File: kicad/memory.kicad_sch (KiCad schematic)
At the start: 12 parts, among them U10 W65C22S, U11 74AC138, U6 Address_Decoder, U7 AS6C4008, U8 AS6C4008, U9 AT28C256

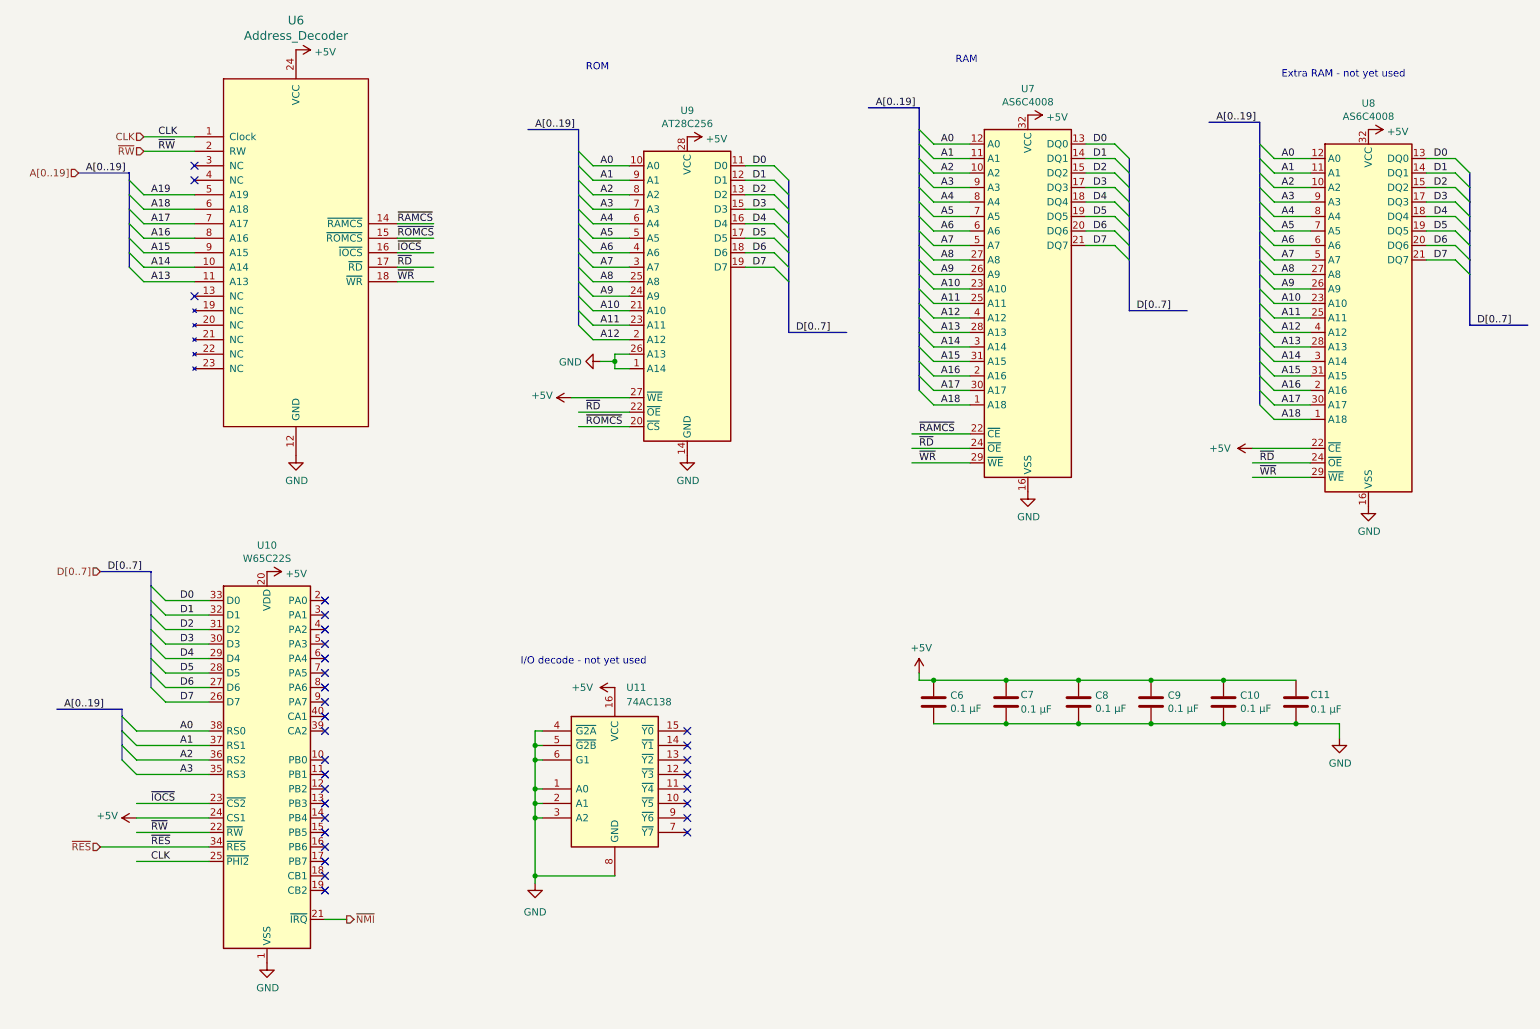
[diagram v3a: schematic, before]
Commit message: update address decoding, extend README
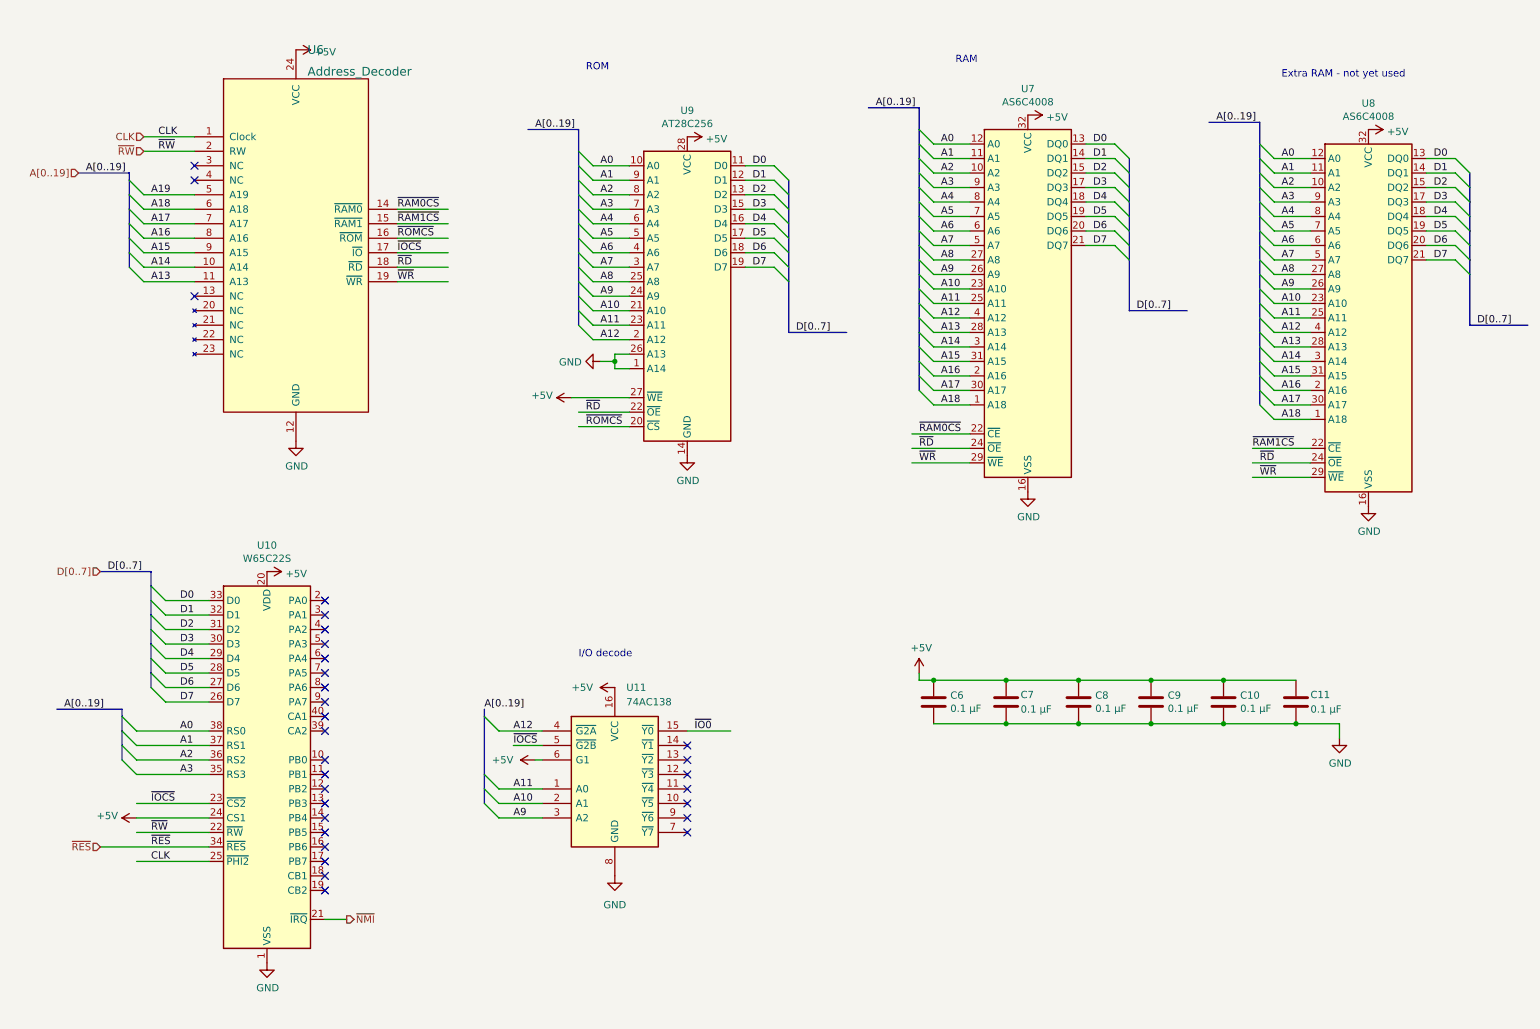
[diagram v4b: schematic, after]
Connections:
- net +5V: now also U11.6 (G1); no longer U8.22 (~{CE})
- net A10: now also U11.2 (A1)
- net A11: now also U11.1 (A0)
- net A12: now also U11.4 (~{G2A})
- net A9: now also U11.3 (A2)
- net GND: no longer U11.1 (A0), U11.2 (A1), U11.3 (A2), U11.4 (~{G2A}), U11.5 (~{G2B}), U11.6 (G1)
- net ~{IOCS}: now also U11.5 (~{G2B}), U6.17 (~{IO}); no longer U6.16 (~{IOCS})
- net ~{RD}: now also U6.18 (~{RD}); no longer U6.17 (~{RD})
- net ~{ROMCS}: now also U6.16 (~{ROM}); no longer U6.15 (~{ROMCS})
- net ~{WR}: now also U6.19 (~{WR}); no longer U6.18 (~{WR})
- net ~{IO0}: now reaches U11.15 (~{Y0})
- net ~{RAMCS} renamed ~{RAM0CS}
- new net ~{RAM1CS}: U6.15 (~{RAM1}), U8.22 (~{CE})
- no-connect marks 31 -> 30
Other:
- note added: "I/O decode"
- note removed: "I/O decode - not yet used"

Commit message: separate I/O schematic page, add SC16C752 for future use
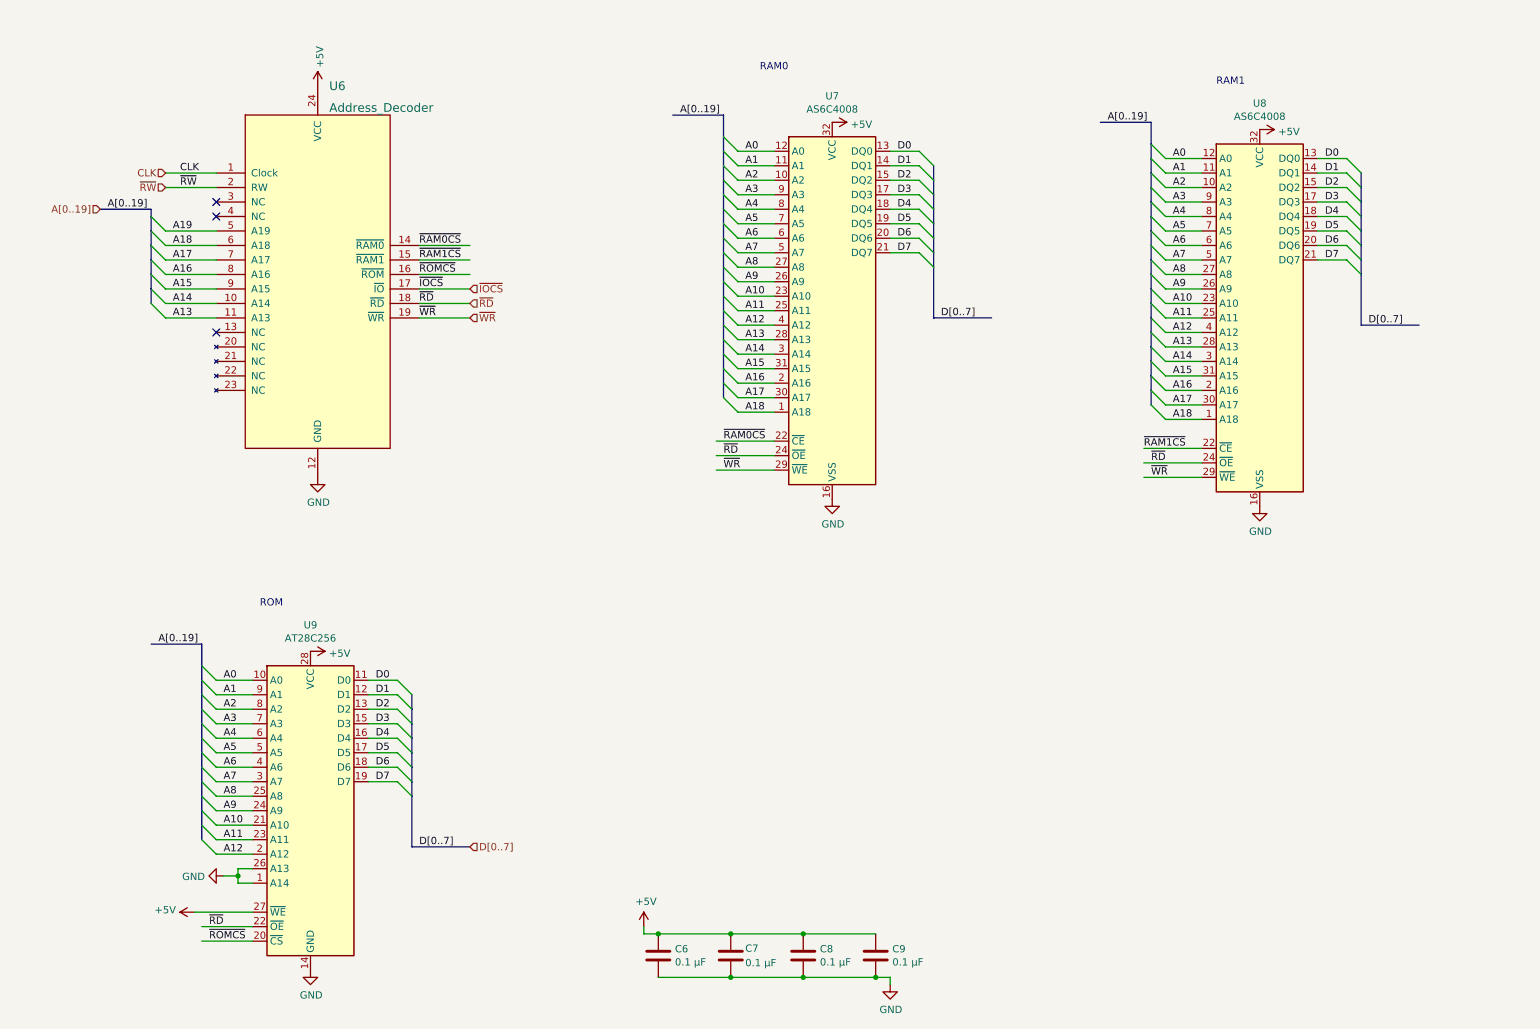
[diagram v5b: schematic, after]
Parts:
- removed C10, C11: 0.1 µF, symbol Device:C
- removed U10: W65C22S, Package_DIP:DIP-40_W15.24mm, symbol project:W65C22S
- removed U11: 74AC138, symbol project:74AC138
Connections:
- no-connect marks 30 -> 3
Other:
- note added: "RAM0"
- note added: "RAM1"
- note removed: "Extra RAM - not yet used"
- note removed: "I/O decode"
- note removed: "RAM"
- moved on the sheet: C6, C7, C8, C9, U7, U8, U9
